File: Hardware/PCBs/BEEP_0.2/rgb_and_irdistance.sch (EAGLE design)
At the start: 5 parts, among them X1 MICROMATCH-8

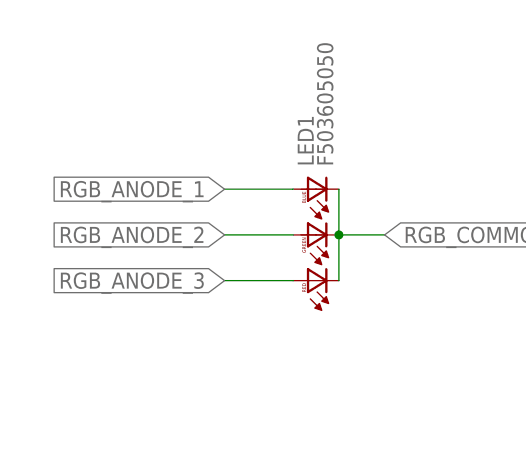
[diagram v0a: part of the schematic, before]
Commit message: enhance routing fix rgb and ir distance board (connector was on the wrong side)
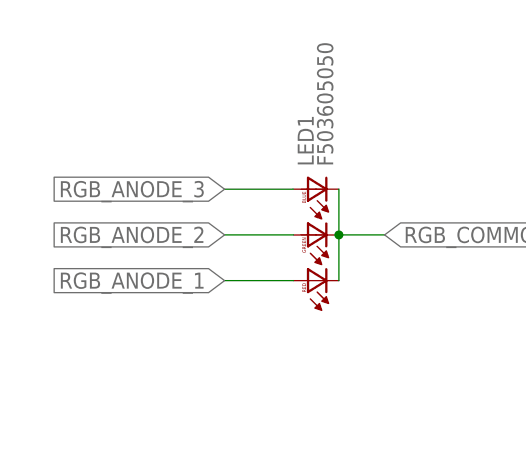
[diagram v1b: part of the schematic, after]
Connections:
- net RGB_ANODE_1: now also LED1.RA; no longer LED1.BA
- net RGB_ANODE_3: now also LED1.BA; no longer LED1.RA
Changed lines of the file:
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@@
 <net name="RGB_ANODE_1" class="0">
-<segment>
-<pinref part="LED1" gate="G$1" pin="BA"/>
-<wire x1="53.34" y1="93.98" x2="45.72" y2="93.98" width="0.1524" layer="91"/>
-<label x="45.72" y="93.98" size="1.778" layer="95" rot="R180" xref="yes"/>
-</segment>
 <segment>
 <wire x1="231.14" y1="78.74" x2="218.44" y2="78.74" width="0.1524" layer="91"/>
 <label x="218.44" y="78.74" size="1.27" layer="95" rot="R180" xref="yes"/>
 <pinref part="X1" gate="-1" pin="S"/>
+</segment>
+<segment>
+<pinref part="LED1" gate="G$1" pin="RA"/>
+<wire x1="53.34" y1="83.82" x2="45.72" y2="83.82" width="0.1524" layer="91"/>
+<label x="45.72" y="83.82" size="1.778" layer="95" rot="R180" xref="yes"/>
 </segment>
 </net>
@@
 <net name="RGB_ANODE_3" class="0">
 <segment>
-<pinref part="LED1" gate="G$1" pin="RA"/>
-<wire x1="53.34" y1="83.82" x2="45.72" y2="83.82" width="0.1524" layer="91"/>
-<label x="45.72" y="83.82" size="1.778" layer="95" rot="R180" xref="yes"/>
-</segment>
-<segment>
 <wire x1="231.14" y1="81.28" x2="218.44" y2="81.28" width="0.1524" layer="91"/>
 <label x="218.44" y="81.28" size="1.27" layer="95" rot="R180" xref="yes"/>
 <pinref part="X1" gate="-2" pin="S"/>
 </segment>
+<segment>
+<pinref part="LED1" gate="G$1" pin="BA"/>
+<wire x1="53.34" y1="93.98" x2="45.72" y2="93.98" width="0.1524" layer="91"/>
+<label x="45.72" y="93.98" size="1.778" layer="95" rot="R180" xref="yes"/>
+</segment>
 </net>

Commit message: rearrange connectors routing
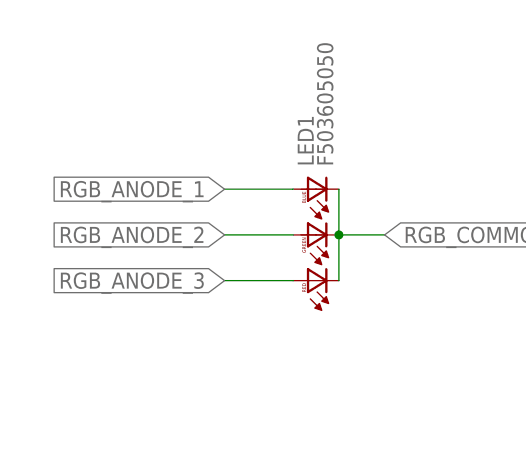
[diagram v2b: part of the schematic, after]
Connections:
- net RGB_ANODE_1: now also LED1.BA; no longer LED1.RA
- net RGB_ANODE_3: now also LED1.RA; no longer LED1.BA
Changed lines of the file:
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@@
 </segment>
 <segment>
-<pinref part="LED1" gate="G$1" pin="RA"/>
-<wire x1="53.34" y1="83.82" x2="45.72" y2="83.82" width="0.1524" layer="91"/>
-<label x="45.72" y="83.82" size="1.778" layer="95" rot="R180" xref="yes"/>
+<pinref part="LED1" gate="G$1" pin="BA"/>
+<wire x1="53.34" y1="93.98" x2="45.72" y2="93.98" width="0.1524" layer="91"/>
+<label x="45.72" y="93.98" size="1.778" layer="95" rot="R180" xref="yes"/>
 </segment>
 </net>
@@
 </segment>
 <segment>
-<pinref part="LED1" gate="G$1" pin="BA"/>
-<wire x1="53.34" y1="93.98" x2="45.72" y2="93.98" width="0.1524" layer="91"/>
-<label x="45.72" y="93.98" size="1.778" layer="95" rot="R180" xref="yes"/>
+<pinref part="LED1" gate="G$1" pin="RA"/>
+<wire x1="53.34" y1="83.82" x2="45.72" y2="83.82" width="0.1524" layer="91"/>
+<label x="45.72" y="83.82" size="1.778" layer="95" rot="R180" xref="yes"/>
 </segment>
 </net>

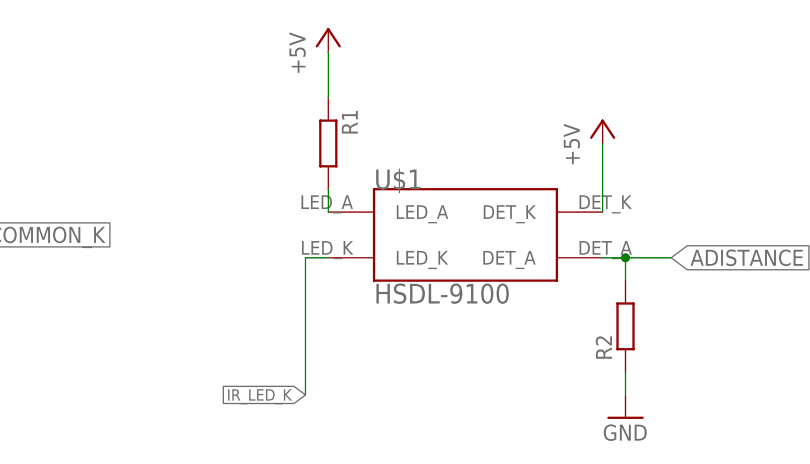
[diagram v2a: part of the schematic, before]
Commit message: move folders try to apply drc from sparkfun (wip) moved audio connetor add slice for camera flexcable
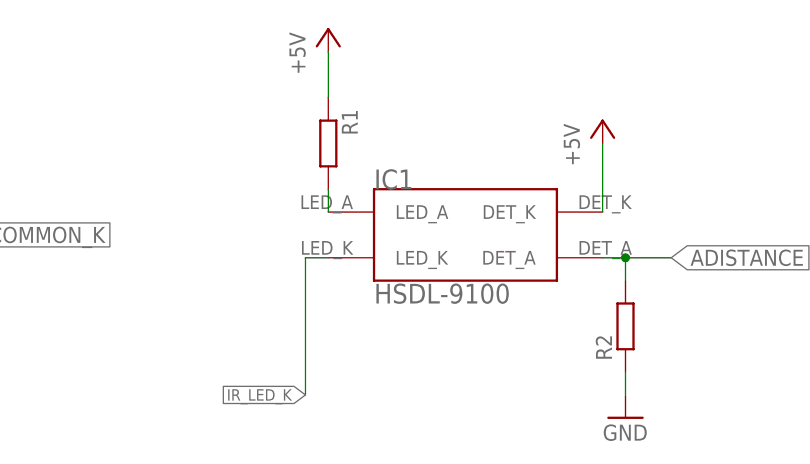
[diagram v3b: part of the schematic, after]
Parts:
- renumbered U$1 to IC1
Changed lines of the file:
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@@
 <part name="X1" library="con-amp-micromatch" deviceset="MICROMATCH-8" device=""/>
 <part name="FRAME1" library="frames" deviceset="A4L-LOC" device=""/>
-<part name="U$1" library="BEEP" deviceset="HSDL-9100" device=""/>
+<part name="IC1" library="BEEP" deviceset="HSDL-9100" device=""/>
 <part name="P+1" library="supply1" deviceset="+5V" device=""/>
 <part name="P+2" library="supply1" deviceset="+5V" device=""/>
@@
 <instance part="X1" gate="-8" x="236.22" y="96.52" rot="R180"/>
 <instance part="FRAME1" gate="G$1" x="0" y="0"/>
-<instance part="U$1" gate="G$1" x="124.46" y="88.9"/>
+<instance part="IC1" gate="G$1" x="124.46" y="88.9"/>
 <instance part="P+1" gate="1" x="139.7" y="101.6"/>
 <instance part="P+2" gate="1" x="223.52" y="104.14"/>
@@
 <junction x="142.24" y="86.36"/>
 <label x="147.32" y="86.36" size="1.778" layer="95" xref="yes"/>
-<pinref part="U$1" gate="G$1" pin="DET_A"/>
+<pinref part="IC1" gate="G$1" pin="DET_A"/>
 </segment>
 <segment>
@@
 <pinref part="R1" gate="G$1" pin="2"/>
 <wire x1="109.22" y1="91.44" x2="109.22" y2="93.98" width="0.1524" layer="91"/>
-<pinref part="U$1" gate="G$1" pin="LED_A"/>
+<pinref part="IC1" gate="G$1" pin="LED_A"/>
 </segment>
 </net>
@@
 <net name="IR_LED_K" class="0">
 <segment>
-<pinref part="U$1" gate="G$1" pin="LED_K"/>
+<pinref part="IC1" gate="G$1" pin="LED_K"/>
 <wire x1="109.22" y1="86.36" x2="106.68" y2="86.36" width="0.1524" layer="91"/>
 <wire x1="106.68" y1="86.36" x2="106.68" y2="71.12" width="0.1524" layer="91"/>
@@
 <segment>
 <wire x1="139.7" y1="91.44" x2="139.7" y2="99.06" width="0.1524" layer="91"/>
-<pinref part="U$1" gate="G$1" pin="DET_K"/>
+<pinref part="IC1" gate="G$1" pin="DET_K"/>
 <pinref part="P+1" gate="1" pin="+5V"/>
 </segment>

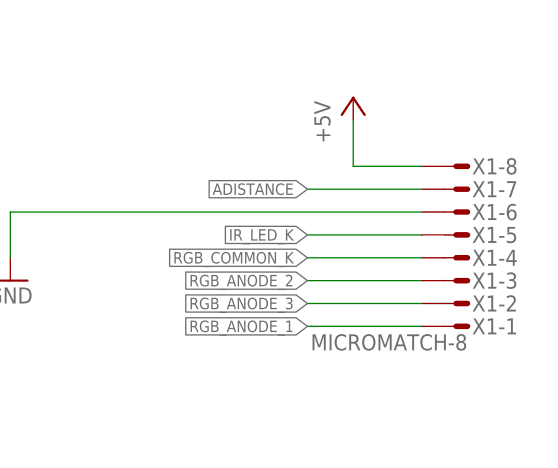
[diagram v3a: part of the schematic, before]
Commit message: continue work on 3D model and replace connector for ir rgb board
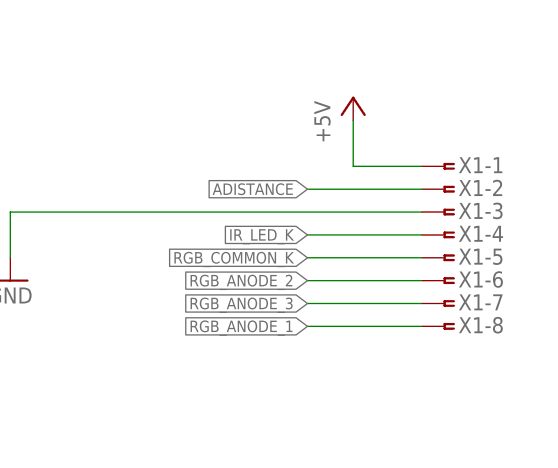
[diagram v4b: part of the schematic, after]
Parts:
- X1: value MICROMATCH-8 -> (none); device con-amp-micromatch:MICROMATCH-8 -> con-amp:FTOP-8
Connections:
- net +5V: now also X1-1.1; no longer X1-8.S
- net ADISTANCE: now also X1-2.1; no longer X1-7.S
- net GND: now also X1-3.1; no longer X1-6.S
- net IR_LED_K: now also X1-4.1; no longer X1-5.S
- net RGB_ANODE_1: now also X1-8.1; no longer X1-1.S
- net RGB_ANODE_2: now also X1-6.1; no longer X1-3.S
- net RGB_ANODE_3: now also X1-7.1; no longer X1-2.S
- net RGB_COMMON_K: now also X1-5.1; no longer X1-4.S
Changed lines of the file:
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@@
 <part name="R1" library="rcl" deviceset="R-EU_" device="R0603"/>
 <part name="R2" library="rcl" deviceset="R-EU_" device="R0603"/>
-<part name="X1" library="con-amp-micromatch" deviceset="MICROMATCH-8" device=""/>
 <part name="FRAME1" library="frames" deviceset="A4L-LOC" device=""/>
 <part name="IC1" library="BEEP" deviceset="HSDL-9100" device=""/>
@@
 <part name="GND1" library="supply1" deviceset="GND" device=""/>
 <part name="GND2" library="supply1" deviceset="GND" device=""/>
+<part name="X1" library="con-amp" deviceset="FTOP-8" device=""/>
 </parts>
 <sheets>
@@
 <instance part="R1" gate="G$1" x="109.22" y="99.06" rot="R270"/>
 <instance part="R2" gate="G$1" x="142.24" y="78.74" rot="R90"/>
-<instance part="X1" gate="-1" x="236.22" y="78.74" rot="R180"/>
-<instance part="X1" gate="-2" x="236.22" y="81.28" rot="R180"/>
-<instance part="X1" gate="-3" x="236.22" y="83.82" rot="R180"/>
-<instance part="X1" gate="-4" x="236.22" y="86.36" rot="R180"/>
-<instance part="X1" gate="-5" x="236.22" y="88.9" rot="R180"/>
-<instance part="X1" gate="-6" x="236.22" y="91.44" rot="R180"/>
-<instance part="X1" gate="-7" x="236.22" y="93.98" rot="R180"/>
-<instance part="X1" gate="-8" x="236.22" y="96.52" rot="R180"/>
 <instance part="FRAME1" gate="G$1" x="0" y="0"/>
 <instance part="IC1" gate="G$1" x="124.46" y="88.9"/>
@@
 <instance part="GND1" gate="1" x="142.24" y="68.58"/>
 <instance part="GND2" gate="1" x="185.42" y="83.82"/>
+<instance part="X1" gate="-1" x="233.68" y="96.52"/>
+<instance part="X1" gate="-2" x="233.68" y="93.98"/>
+<instance part="X1" gate="-3" x="233.68" y="91.44"/>
+<instance part="X1" gate="-4" x="233.68" y="88.9"/>
+<instance part="X1" gate="-5" x="233.68" y="86.36"/>
+<instance part="X1" gate="-6" x="233.68" y="83.82"/>
+<instance part="X1" gate="-7" x="233.68" y="81.28"/>
+<instance part="X1" gate="-8" x="233.68" y="78.74"/>
 </instances>
 <busses>
@@
 <wire x1="231.14" y1="86.36" x2="218.44" y2="86.36" width="0.1524" layer="91"/>
 <label x="218.44" y="86.36" size="1.27" layer="95" rot="R180" xref="yes"/>
-<pinref part="X1" gate="-4" pin="S"/>
+<pinref part="X1" gate="-5" pin="1"/>
 </segment>
 </net>
@@
 <wire x1="231.14" y1="93.98" x2="218.44" y2="93.98" width="0.1524" layer="91"/>
 <label x="218.44" y="93.98" size="1.27" layer="95" rot="R180" xref="yes"/>
-<pinref part="X1" gate="-7" pin="S"/>
+<pinref part="X1" gate="-2" pin="1"/>
 </segment>
 </net>
@@
 <wire x1="231.14" y1="78.74" x2="218.44" y2="78.74" width="0.1524" layer="91"/>
 <label x="218.44" y="78.74" size="1.27" layer="95" rot="R180" xref="yes"/>
-<pinref part="X1" gate="-1" pin="S"/>
+<pinref part="X1" gate="-8" pin="1"/>
 </segment>
 <segment>
@@
 <wire x1="231.14" y1="83.82" x2="218.44" y2="83.82" width="0.1524" layer="91"/>
 <label x="218.44" y="83.82" size="1.27" layer="95" rot="R180" xref="yes"/>
-<pinref part="X1" gate="-3" pin="S"/>
+<pinref part="X1" gate="-6" pin="1"/>
 </segment>
 </net>
@@
 <wire x1="231.14" y1="81.28" x2="218.44" y2="81.28" width="0.1524" layer="91"/>
 <label x="218.44" y="81.28" size="1.27" layer="95" rot="R180" xref="yes"/>
-<pinref part="X1" gate="-2" pin="S"/>
+<pinref part="X1" gate="-7" pin="1"/>
 </segment>
 <segment>
@@
 </segment>
 <segment>
-<pinref part="X1" gate="-5" pin="S"/>
 <wire x1="231.14" y1="88.9" x2="218.44" y2="88.9" width="0.1524" layer="91"/>
 <label x="218.44" y="88.9" size="1.27" layer="95" rot="R180" xref="yes"/>
+<pinref part="X1" gate="-4" pin="1"/>
 </segment>
 </net>
@@
 <wire x1="231.14" y1="96.52" x2="223.52" y2="96.52" width="0.1524" layer="91"/>
 <wire x1="223.52" y1="96.52" x2="223.52" y2="101.6" width="0.1524" layer="91"/>
-<pinref part="X1" gate="-8" pin="S"/>
 <pinref part="P+2" gate="1" pin="+5V"/>
+<pinref part="X1" gate="-1" pin="1"/>
 </segment>
 </net>
@@
 <segment>
 <pinref part="GND2" gate="1" pin="GND"/>
-<pinref part="X1" gate="-6" pin="S"/>
 <wire x1="231.14" y1="91.44" x2="185.42" y2="91.44" width="0.1524" layer="91"/>
 <wire x1="185.42" y1="91.44" x2="185.42" y2="86.36" width="0.1524" layer="91"/>
+<pinref part="X1" gate="-3" pin="1"/>
 </segment>
 </net>

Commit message: modelling 3D model of case, minor change of ir / rgb board
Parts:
- R1, R2: device rcl:R-EU_R0603 -> resistor:R-EU_M0805
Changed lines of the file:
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@@
 <?xml version="1.0" encoding="utf-8"?>
 <!DOCTYPE eagle SYSTEM "eagle.dtd">
-<eagle version="6.4">
+<eagle version="6.5.0">
 <drawing>
 <settings>
@@
 <parts>
 <part name="LED1" library="BEEP" deviceset="F50360" device="5050"/>
-<part name="R1" library="rcl" deviceset="R-EU_" device="R0603"/>
-<part name="R2" library="rcl" deviceset="R-EU_" device="R0603"/>
+<part name="R1" library="resistor" deviceset="R-EU_" device="M0805"/>
+<part name="R2" library="resistor" deviceset="R-EU_" device="M0805"/>
 <part name="FRAME1" library="frames" deviceset="A4L-LOC" device=""/>
 <part name="IC1" library="BEEP" deviceset="HSDL-9100" device=""/>
@@
 <net name="RGB_ANODE_1" class="0">
 <segment>
+<pinref part="LED1" gate="G$1" pin="BA"/>
+<wire x1="53.34" y1="93.98" x2="45.72" y2="93.98" width="0.1524" layer="91"/>
+<label x="45.72" y="93.98" size="1.778" layer="95" rot="R180" xref="yes"/>
+</segment>
+<segment>
 <wire x1="231.14" y1="78.74" x2="218.44" y2="78.74" width="0.1524" layer="91"/>
 <label x="218.44" y="78.74" size="1.27" layer="95" rot="R180" xref="yes"/>
 <pinref part="X1" gate="-8" pin="1"/>
 </segment>
-<segment>
-<pinref part="LED1" gate="G$1" pin="BA"/>
-<wire x1="53.34" y1="93.98" x2="45.72" y2="93.98" width="0.1524" layer="91"/>
-<label x="45.72" y="93.98" size="1.778" layer="95" rot="R180" xref="yes"/>
-</segment>
 </net>
 <net name="RGB_ANODE_2" class="0">
@@
 <net name="RGB_ANODE_3" class="0">
 <segment>
+<pinref part="LED1" gate="G$1" pin="RA"/>
+<wire x1="53.34" y1="83.82" x2="45.72" y2="83.82" width="0.1524" layer="91"/>
+<label x="45.72" y="83.82" size="1.778" layer="95" rot="R180" xref="yes"/>
+</segment>
+<segment>
 <wire x1="231.14" y1="81.28" x2="218.44" y2="81.28" width="0.1524" layer="91"/>
 <label x="218.44" y="81.28" size="1.27" layer="95" rot="R180" xref="yes"/>
 <pinref part="X1" gate="-7" pin="1"/>
 </segment>
-<segment>
-<pinref part="LED1" gate="G$1" pin="RA"/>
-<wire x1="53.34" y1="83.82" x2="45.72" y2="83.82" width="0.1524" layer="91"/>
-<label x="45.72" y="83.82" size="1.778" layer="95" rot="R180" xref="yes"/>
-</segment>
-</net>
+</net>
